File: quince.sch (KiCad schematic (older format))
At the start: 115 parts, among them J1 NEIGHBOR1, J19 GND, J2 NEIGHBOR2, J3 RFIN, J7 BONUS_ROW, J8 LO, U1 TLV3502, U2 AD8347, U3 SAW FILTER, U4 LNA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

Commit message: fix U1 part selection
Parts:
- U1: Description IC COMPARATOR R-R HI-SPD SOT23-8 -> IC COMPARATOR R-R HI-SPD 8-SOIC; Part Number TLV3502AIDCNR -> TLV3502AIDR
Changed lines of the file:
@@
 F 3 "" H 11850 3600 60  0001 C CNN
 F 4 "Texas Instruments" H 11850 3600 50  0001 C CNN "Manufacturer"
-F 5 "TLV3502AIDCNR" H 11850 3600 50  0001 C CNN "Part Number"
-F 6 "IC COMPARATOR R-R HI-SPD SOT23-8" H 11850 3600 50  0001 C CNN "Description"
+F 5 "TLV3502AIDR" H 11850 3600 50  0001 C CNN "Part Number"
+F 6 "IC COMPARATOR R-R HI-SPD 8-SOIC" H 11850 3600 50  0001 C CNN "Description"
 	1    11850 3600
 	1    0    0    -1

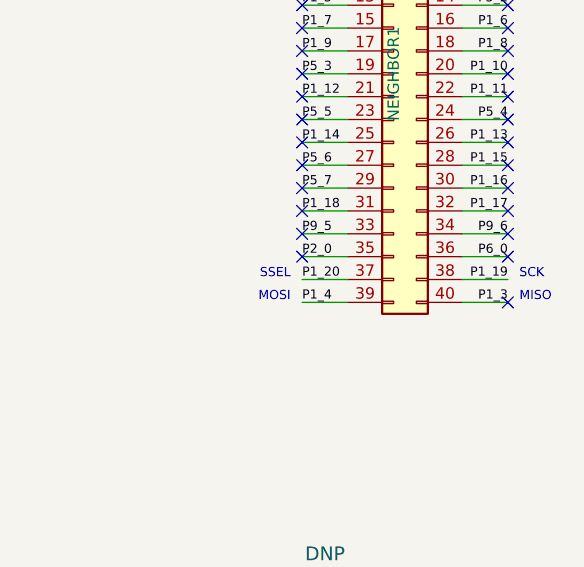
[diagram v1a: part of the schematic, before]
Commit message: adopt OSHWA convention for SPI signal names https://www.oshwa.org/a-resolution-to-redefine-spi-signal-names
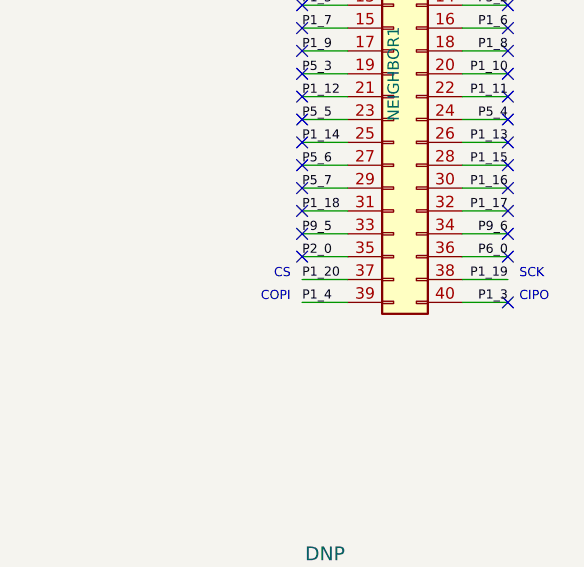
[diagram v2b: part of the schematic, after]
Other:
- note added: "CIPO"
- note added: "COPI"
- note added: "CS"
- note removed: "MISO"
- note removed: "MOSI"
- note removed: "SSEL"
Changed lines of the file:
@@
 P2_0
 Text Notes 16150 7050 0    40   ~ 0
-MISO
+CIPO
 Text Notes 15150 7050 2    40   ~ 0
-MOSI
+COPI
 Text Notes 16150 6950 0    40   ~ 0
 SCK
 Text Notes 15150 6950 2    40   ~ 0
-SSEL
+CS
 Text Label 16200 4700 2    40   ~ 0
 I2C0_SCL
